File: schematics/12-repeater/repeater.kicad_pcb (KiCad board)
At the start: 4 copper layers, 50 x 25 mm, 13 parts, among them J1 Cat5, J2 PSG01571, U1 PCA9600D

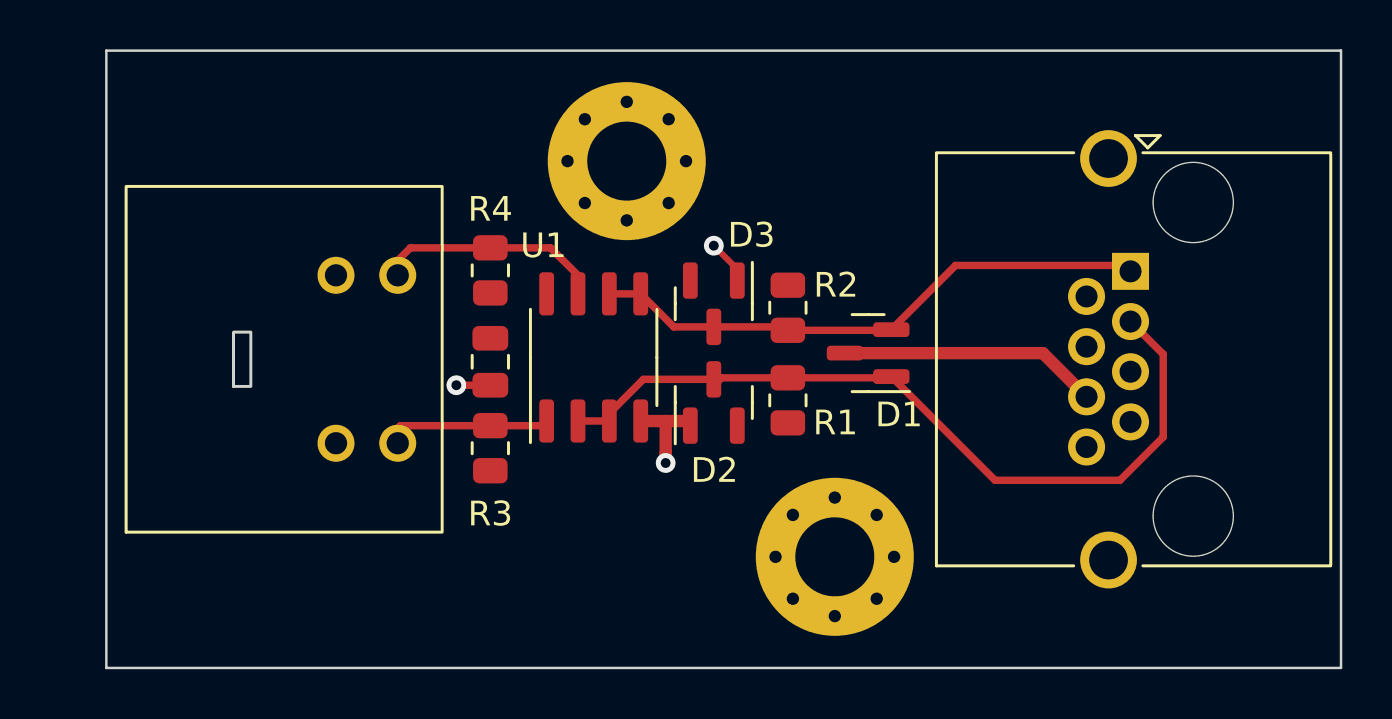
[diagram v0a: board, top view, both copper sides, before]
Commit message: Replace mini-DIN with more well-documented part
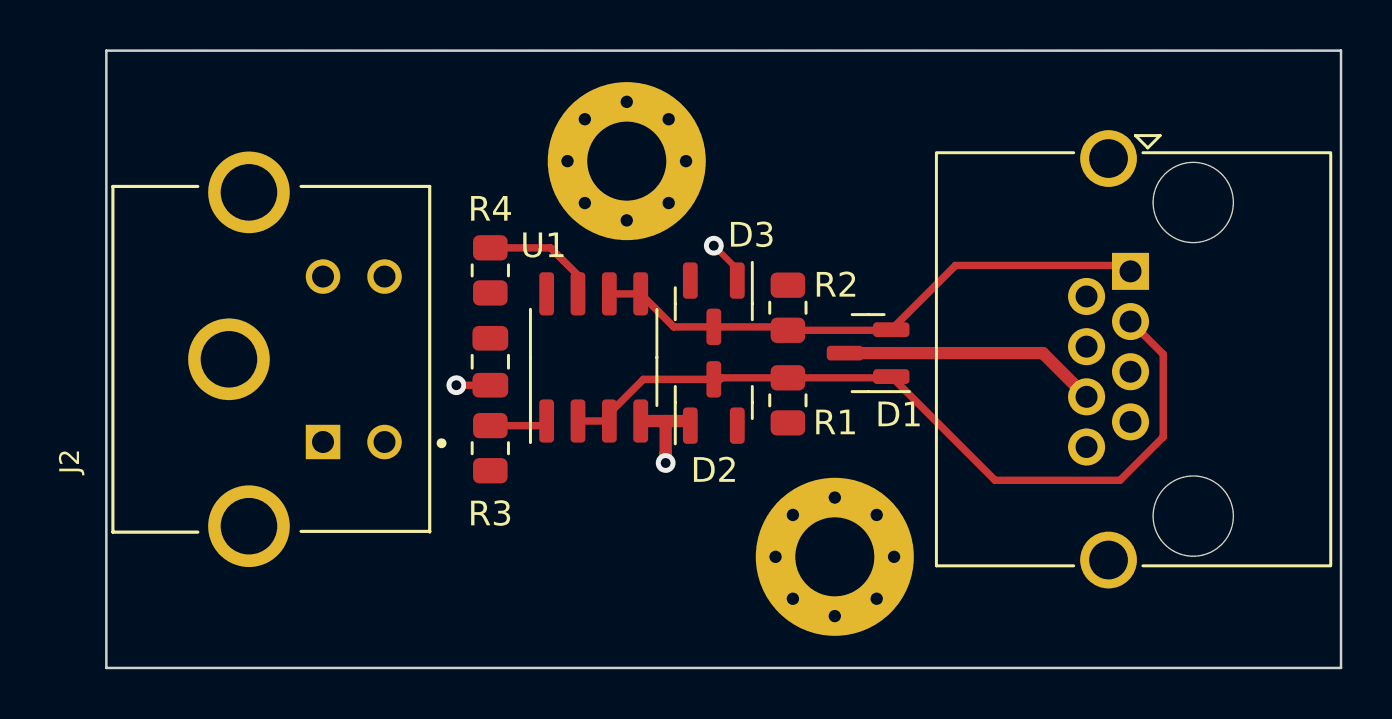
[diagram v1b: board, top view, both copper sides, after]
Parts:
- J2: value PSG01571 -> Mini-DIN; footprint royale:Mini-Din-Through-Hole -> royale:TE_5749181-1
- moved J2 10.6 mm to (127.9, 115.5)
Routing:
- net /SCL: track 9.44 -> 4.76 mm
- net /SDA: track 6.87 -> 2.36 mm
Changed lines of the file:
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@@
   (net 5 "/SDA")
   (net 6 "/SCL")
+  (footprint "royale:TE_5749181-1" (layer "F.Cu")
+    (at 127.875 115.5 90)
+    (property "Sheetfile" "repeater.kicad_sch")
+    (property "Sheetname" "")
+    (attr through_hole)
+    (fp_text reference "J2" (at -4.132295 -10.253715 90) (layer "F.SilkS")
+      (effects (font (size 0.800449 0.800449) (thickness 0.15)))
+    )
+    (fp_text value "Mini-DIN" (at -0.57404 7.25231 90) (layer "F.Fab")
+      (effects (font (size 0.800031 0.800031) (thickness 0.15)))
+    )
+    (fp_line (start -7 -5.07) (end -7 -8.51) (layer "F.SilkS") (width 0.127))
+    (fp_line (start 7 -5.07) (end 7 -8.51) (layer "F.SilkS") (width 0.127))
+    (fp_line (start 7 4.32) (end -6.97 4.32) (layer "F.SilkS") (width 0.127))
+    (fp_line (start -6.97 -0.89) (end -6.97 4.32) (layer "F.SilkS") (width 0.127))
+    (fp_line (start -6.97 4.32) (end -7 4.32) (layer "F.SilkS") (width 0.127))
+    (fp_line (start -7 -8.51) (end 7 -8.51) (layer "F.SilkS") (width 0.127))
+    (fp_line (start 7 -0.89) (end 7 4.32) (layer "F.SilkS") (width 0.127))
+    (fp_circle (center -3.4 4.8) (end -3.3 4.8) (layer "F.SilkS") (width 0.2) (fill none))
+    (fp_line (start 7.25 -8.76) (end 7.25 4.57) (layer "F.CrtYd") (width 0.05))
+    (fp_line (start 7.25 4.57) (end -7.25 4.57) (layer "F.CrtYd") (width 0.05))
+    (fp_line (start -7.25 -8.76) (end 7.25 -8.76) (layer "F.CrtYd") (width 0.05))
+    (fp_line (start -7.25 4.57) (end -7.25 -8.76) (layer "F.CrtYd") (width 0.05))
+    (fp_line (start 7 -8.51) (end 7 4.32) (layer "F.Fab") (width 0.127))
+    (fp_line (start -7 4.32) (end -7 -8.51) (layer "F.Fab") (width 0.127))
+    (fp_line (start 7 4.32) (end -7 4.32) (layer "F.Fab") (width 0.127))
+    (fp_line (start -7 -8.51) (end 7 -8.51) (layer "F.Fab") (width 0.127))
+    (pad "1" thru_hole rect (at -3.35 0 90) (size 1.398 1.398) (drill 0.89) (layers *.Cu *.Mask)
+      (net 2 "GND") (pintype "passive"))
+    (pad "2" thru_hole circle (at 3.35 0 90) (size 1.398 1.398) (drill 0.89) (layers *.Cu *.Mask)
+      (net 1 "1v8") (pintype "passive"))
+    (pad "3" thru_hole circle (at -3.35 2.49 90) (size 1.398 1.398) (drill 0.89) (layers *.Cu *.Mask)
+      (net 6 "/SCL") (pintype "passive"))
+    (pad "4" thru_hole circle (at 3.35 2.49 90) (size 1.398 1.398) (drill 0.89) (layers *.Cu *.Mask)
+      (net 5 "/SDA") (pintype "passive"))
+    (pad "5" thru_hole circle (at -6.76 -3 90) (size 3.306 3.306) (drill 2.29) (layers *.Cu *.Mask)
+      (net 2 "GND") (pintype "input"))
+    (pad "5" thru_hole circle (at 0 -3.81 90) (size 3.306 3.306) (drill 2.29) (layers *.Cu *.Mask)
+      (net 2 "GND") (pintype "input"))
+    (pad "5" thru_hole circle (at 6.76 -3 90) (size 3.306 3.306) (drill 2.29) (layers *.Cu *.Mask)
+      (net 2 "GND") (pintype "input"))
+    (model "${KIPRJMOD}/../00-lib/royale.models/5749181-1.STEP"
+      (offset (xyz 0 8.5 6.5))
+      (scale (xyz 1 1 1))
+      (rotate (xyz 90 180 0))
+    )
+  )
   (footprint "Resistor_SMD:R_0805_2012Metric" (layer "F.Cu")
     (at 146.7 117.1625 90)
@@
     (pad "8" smd roundrect (at 2.575 -1.905 90) (size 1.75 0.6) (layers "F.Cu" "F.Paste" "F.Mask") (roundrect_rratio 0.25)
       (net 1 "1v8") (pinfunction "VCC") (pintype "power_in"))
-    (model "${KICAD6_3DMODEL_DIR}/Package_SO.3dshapes/SO-8_3.9x4.9mm_P1.27mm.wrl"
+    (model "${KICAD6_3DMODEL_DIR}/Package_SO.3dshapes/SOIC-8_3.9x4.9mm_P1.27mm.step"
       (offset (xyz 0 0 0))
       (scale (xyz 1 1 1))
@@
       (rotate (xyz 0 0 0))
     )
-  )
-  (footprint "royale:Mini-Din-Through-Hole" (layer "F.Cu")
-    (at 119.9 122.5 90)
-    (property "Farnell" "1280736")
-    (property "Sheetfile" "repeater.kicad_sch")
-    (property "Sheetname" "")
-    (attr through_hole)
-    (fp_text reference "J2" (at 3.405 -4.195 90 unlocked) (layer "F.Fab")
-      (effects (font (size 1 1) (thickness 0.15)))
-    )
-    (fp_text value "PSG01571" (at -5.08 -5.08 90 unlocked) (layer "F.Fab")
-      (effects (font (size 1 1) (thickness 0.15)))
-    )
-    (fp_text user "${REFERENCE}" (at -5.08 -2.54 90 unlocked) (layer "F.Fab")
-      (effects (font (size 1 1) (thickness 0.15)))
-    )
-    (fp_rect (start 0 0) (end 14 12.8) (layer "F.SilkS") (width 0.12) (fill none))
-    (fp_rect (start 5.9 4.35) (end 8.1 5.05) (layer "Edge.Cuts") (width 0.12) (fill none))
-    (pad "1" thru_hole circle (at 3.6 8.5 90) (size 1.5 1.5) (drill 0.9) (layers *.Cu *.Mask)
-      (net 2 "GND") (pintype "passive"))
-    (pad "2" thru_hole circle (at 10.4 8.5 90) (size 1.5 1.5) (drill 0.9) (layers *.Cu *.Mask)
-      (net 1 "1v8") (pintype "passive"))
-    (pad "3" thru_hole circle (at 10.4 11 90) (size 1.5 1.5) (drill 0.9) (layers *.Cu *.Mask)
-      (net 6 "/SCL") (pintype "passive"))
-    (pad "4" thru_hole circle (at 3.6 11 90) (size 1.5 1.5) (drill 0.9) (layers *.Cu *.Mask)
-      (net 5 "/SDA") (pintype "passive"))
   )
   (footprint "Resistor_SMD:R_0805_2012Metric" (layer "F.Cu")
@@
   (segment (start 160.335 111.7) (end 160.575 111.94) (width 0.3) (layer "F.Cu") (net 4))
   (segment (start 143.7 114.1875) (end 146.5625 114.1875) (width 0.3) (layer "F.Cu") (net 4))
-  (segment (start 131.0125 118.1875) (end 134.65 118.1875) (width 0.3) (layer "F.Cu") (net 5))
   (segment (start 136.7425 118.1875) (end 136.93 118) (width 0.3) (layer "F.Cu") (net 5))
-  (segment (start 130.395 118.805) (end 131.0125 118.1875) (width 0.3) (layer "F.Cu") (net 5))
   (segment (start 134.65 118.1875) (end 136.7425 118.1875) (width 0.3) (layer "F.Cu") (net 5))
   (segment (start 138.2 112.1) (end 138.2 112.85) (width 0.3) (layer "F.Cu") (net 6))
-  (segment (start 134.65 110.9875) (end 131.4125 110.9875) (width 0.3) (layer "F.Cu") (net 6))
   (segment (start 134.65 110.9875) (end 137.0875 110.9875) (width 0.3) (layer "F.Cu") (net 6))
   (segment (start 137.0875 110.9875) (end 138.2 112.1) (width 0.3) (layer "F.Cu") (net 6))
-  (segment (start 131.4125 110.9875) (end 130.395 112.005) (width 0.3) (layer "F.Cu") (net 6))
   (zone (net 1) (net_name "1v8") (layer "F.Cu") (hatch edge 0.508)
     (connect_pads (clearance 0.508))

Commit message: Minor cleanup to accomodate new connector
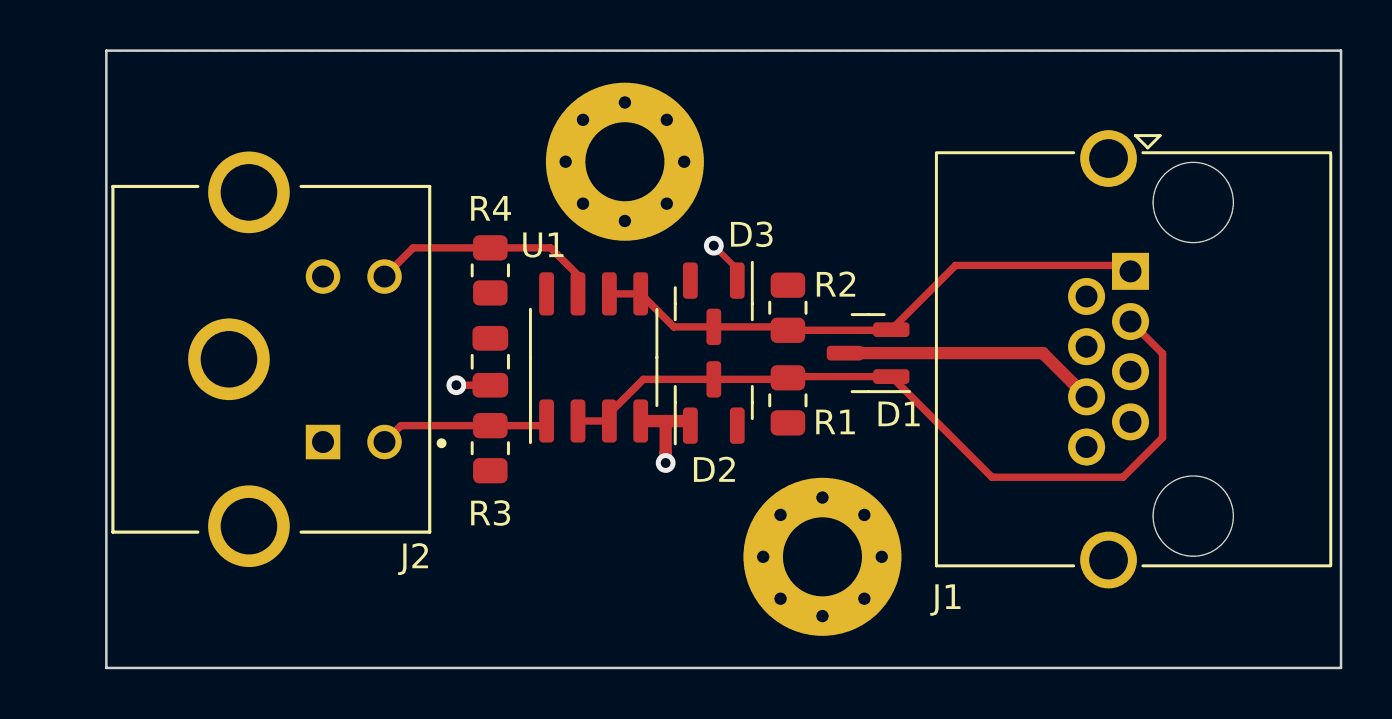
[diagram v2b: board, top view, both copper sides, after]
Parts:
- moved H2 0.50 mm to (148.1, 123.5)
- moved H1 0.08 mm to (140.1, 107.5)
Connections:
- J2 pad 3: /SCL -> /SDA
- J2 pad 4: /SDA -> /SCL
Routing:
- net /SCL: track 4.76 -> 9.53 mm
- net /SDA: track 2.36 -> 6.92 mm

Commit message: Fix minor symbol errors
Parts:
- H1, H2: footprint royale:MountingHole_Pad -> royale:MountingHole_3.2mm_M3_Pad_Via
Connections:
- net 1v8 renamed 5v
- D2 pad 2: (no net) -> unconnected-(D2-Pad2)
- D3 pad 2: (no net) -> unconnected-(D3-Pad2)

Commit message: Reorder RJ45 pins to simplify board layout
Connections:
- J1 pad 1: /SCL_D -> GND
- J1 pad 2: GND -> /SCL_D
- J1 pad 3: /SDA_D -> GND
- J1 pad 4: 5v -> GND
- J1 pad 6: GND -> 5v
- J1 pad 8: GND -> /SDA_D
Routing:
- net /SDA_D: track 32.2 -> 22.7 mm
- net GND: track 17.5 -> 10.1 mm, vias 3 -> 4
- net /SCL_D: track 22.9 -> 20.5 mm
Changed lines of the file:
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@@
     (pad "" np_thru_hole circle (at -2.79 -2.54 270) (size 3.25 3.25) (drill 3.25) (layers *.Cu *.Mask))
     (pad "1" thru_hole rect (at 0 0 270) (size 1.5 1.5) (drill 0.89) (layers *.Cu *.Mask)
+      (net 2 "GND") (pintype "passive"))
+    (pad "2" thru_hole circle (at 1.016 1.78 270) (size 1.5 1.5) (drill 0.89) (layers *.Cu *.Mask)
       (net 4 "/SCL_D") (pintype "passive"))
-    (pad "2" thru_hole circle (at 1.016 1.78 270) (size 1.5 1.5) (drill 0.89) (layers *.Cu *.Mask)
-      (net 2 "GND") (pintype "passive"))
     (pad "3" thru_hole circle (at 2.032 0 270) (size 1.5 1.5) (drill 0.89) (layers *.Cu *.Mask)
-      (net 3 "/SDA_D") (pintype "passive"))
+      (net 2 "GND") (pintype "passive"))
     (pad "4" thru_hole circle (at 3.048 1.78 270) (size 1.5 1.5) (drill 0.89) (layers *.Cu *.Mask)
-      (net 1 "5v") (pintype "passive"))
+      (net 2 "GND") (pintype "passive"))
     (pad "5" thru_hole circle (at 4.064 0 270) (size 1.5 1.5) (drill 0.89) (layers *.Cu *.Mask)
       (net 1 "5v") (pintype "passive"))
     (pad "6" thru_hole circle (at 5.08 1.78 270) (size 1.5 1.5) (drill 0.89) (layers *.Cu *.Mask)
-      (net 2 "GND") (pintype "passive"))
+      (net 1 "5v") (pintype "passive"))
     (pad "7" thru_hole circle (at 6.096 0 270) (size 1.5 1.5) (drill 0.89) (layers *.Cu *.Mask)
       (net 2 "GND") (pintype "passive"))
     (pad "8" thru_hole circle (at 7.112 1.78 270) (size 1.5 1.5) (drill 0.89) (layers *.Cu *.Mask)
-      (net 2 "GND") (pintype "passive"))
+      (net 3 "/SDA_D") (pintype "passive"))
     (pad "SH" thru_hole circle (at -4.57 0.89 270) (size 2.3 2.3) (drill 1.57) (layers *.Cu *.Mask)
       (net 2 "GND") (pintype "passive"))
@@
   (segment (start 140.74 118) (end 141.75 118) (width 0.5) (layer "F.Cu") (net 2))
   (segment (start 142.5625 118) (end 142.75 118.1875) (width 0.5) (layer "F.Cu") (net 2))
+  (segment (start 149.0125 115.25) (end 152.15 115.25) (width 0.25) (layer "F.Cu") (net 2))
   (segment (start 144.65 111.85) (end 143.7 110.9) (width 0.25) (layer "F.Cu") (net 2))
-  (segment (start 149.0125 115.25) (end 157.025 115.25) (width 0.5) (layer "F.Cu") (net 2))
-  (segment (start 157.025 115.25) (end 158.795 117.02) (width 0.5) (layer "F.Cu") (net 2))
   (segment (start 141.75 119.3) (end 141.75 119.7) (width 0.5) (layer "F.Cu") (net 2))
   (segment (start 141.75 118) (end 142.5625 118) (width 0.5) (layer "F.Cu") (net 2))
@@
   (via (at 143.7 110.9) (size 0.8) (drill 0.4) (layers "F.Cu" "B.Cu") (net 2))
   (via (at 133.275 116.55) (size 0.8) (drill 0.4) (layers "F.Cu" "B.Cu") (net 2))
-  (segment (start 161.875 115.272) (end 160.575 113.972) (width 0.3) (layer "F.Cu") (net 3))
-  (segment (start 160.275 120.275) (end 161.875 118.675) (width 0.3) (layer "F.Cu") (net 3))
-  (segment (start 154.9625 120.275) (end 160.275 120.275) (width 0.3) (layer "F.Cu") (net 3))
-  (segment (start 161.875 118.675) (end 161.875 115.272) (width 0.3) (layer "F.Cu") (net 3))
+  (via (at 152.15 115.25) (size 0.8) (drill 0.4) (layers "F.Cu" "B.Cu") (net 2))
   (segment (start 146.75 116.2) (end 150.8875 116.2) (width 0.3) (layer "F.Cu") (net 3))
   (segment (start 139.47 118) (end 139.47 117.688573) (width 0.3) (layer "F.Cu") (net 3))
@@
   (segment (start 146.7 116.25) (end 146.75 116.2) (width 0.3) (layer "F.Cu") (net 3))
   (segment (start 146.6375 116.3125) (end 146.7 116.25) (width 0.3) (layer "F.Cu") (net 3))
-  (segment (start 150.8875 116.2) (end 154.9625 120.275) (width 0.3) (layer "F.Cu") (net 3))
+  (segment (start 150.8875 116.2) (end 155.943 116.2) (width 0.3) (layer "F.Cu") (net 3))
   (segment (start 139.47 117.688573) (end 140.846073 116.3125) (width 0.3) (layer "F.Cu") (net 3))
-  (segment (start 153.4875 111.7) (end 160.335 111.7) (width 0.3) (layer "F.Cu") (net 4))
+  (segment (start 155.943 116.2) (end 158.795 119.052) (width 0.3) (layer "F.Cu") (net 3))
   (segment (start 139.47 112.85) (end 140.74 112.85) (width 0.3) (layer "F.Cu") (net 4))
   (segment (start 140.74 112.85) (end 142.0775 114.1875) (width 0.3) (layer "F.Cu") (net 4))
@@
   (segment (start 150.8625 114.325) (end 150.8875 114.3) (width 0.3) (layer "F.Cu") (net 4))
   (segment (start 146.5625 114.1875) (end 146.7 114.325) (width 0.3) (layer "F.Cu") (net 4))
-  (segment (start 150.8875 114.3) (end 153.4875 111.7) (width 0.3) (layer "F.Cu") (net 4))
-  (segment (start 160.335 111.7) (end 160.575 111.94) (width 0.3) (layer "F.Cu") (net 4))
   (segment (start 143.7 114.1875) (end 146.5625 114.1875) (width 0.3) (layer "F.Cu") (net 4))
+  (segment (start 150.8875 114.3) (end 157.451 114.3) (width 0.3) (layer "F.Cu") (net 4))
+  (segment (start 157.451 114.3) (end 158.795 112.956) (width 0.3) (layer "F.Cu") (net 4))
   (segment (start 134.65 118.1875) (end 131.0275 118.1875) (width 0.3) (layer "F.Cu") (net 5))
   (segment (start 131.0275 118.1875) (end 130.365 118.85) (width 0.3) (layer "F.Cu") (net 5))
